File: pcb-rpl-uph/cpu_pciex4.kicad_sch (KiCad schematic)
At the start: 3 parts, among them U5 RPL_UPH_FCBGA1744

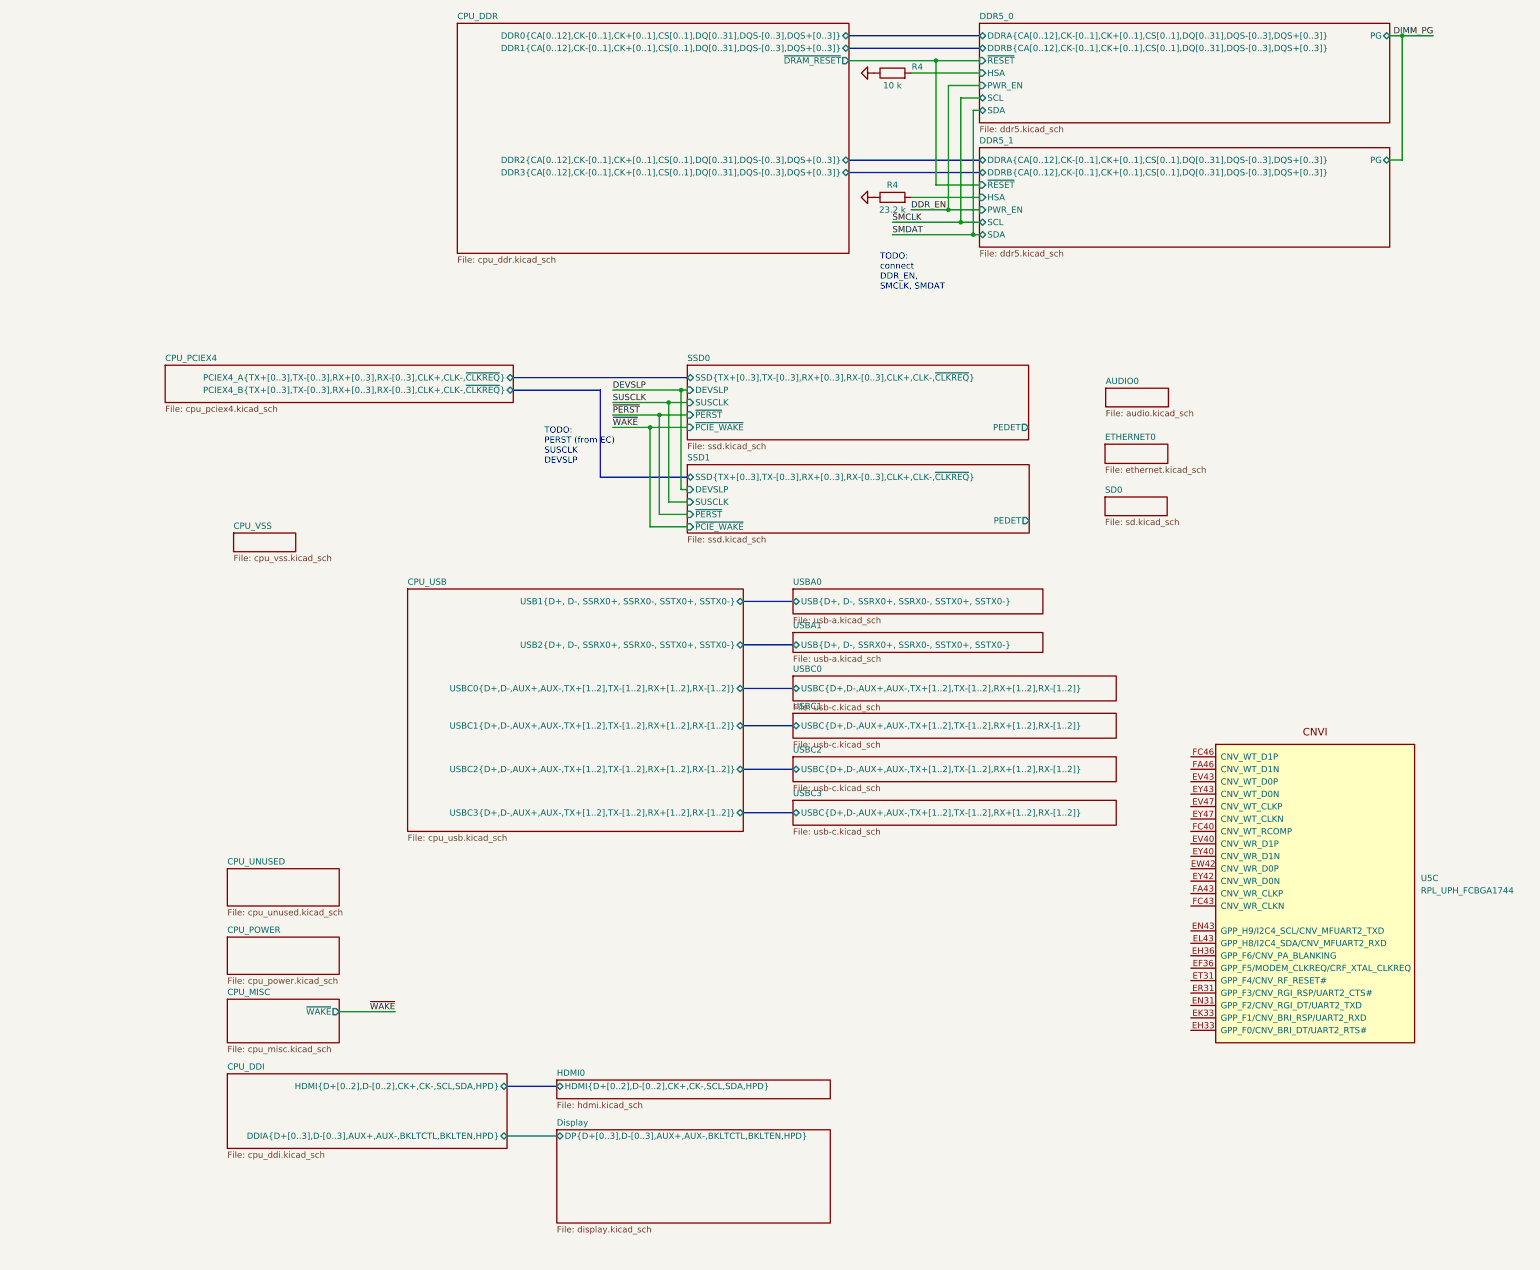
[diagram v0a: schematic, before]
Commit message: refactor much of CPU schematic symbol
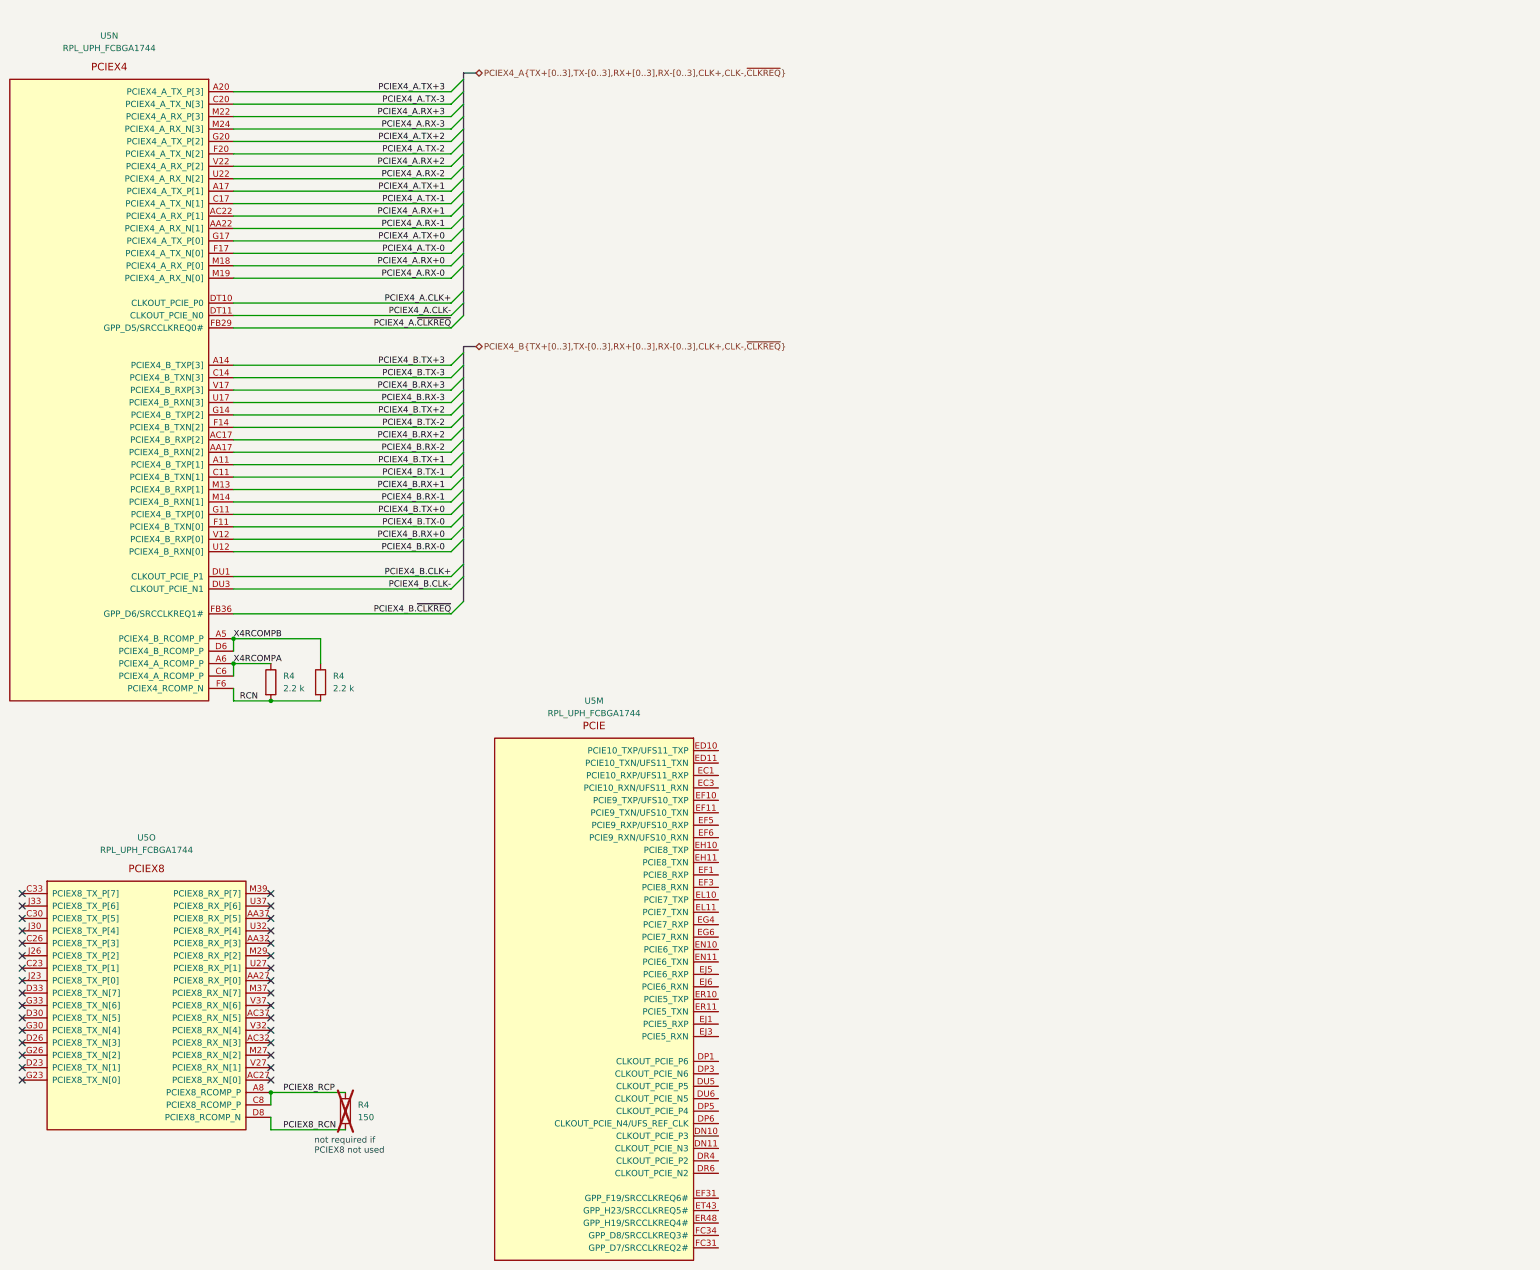
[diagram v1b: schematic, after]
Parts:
- removed R4: 23.2 k, local:R_0201_0603Metric, symbol Device:R
- removed R4: 10 k, local:R_0201_0603Metric, symbol Device:R
- removed U5: RPL_UPH_FCBGA1744, local:RPL_UPH_FCBGA1744, symbol local:RPL_UPH_FCBGA1744
- added R4 (x2): 2.2 k, local:R_0201_0603Metric, symbol Device:R
- added R4: 150, local:R_0201_0603Metric, symbol Device:R
- added U5: RPL_UPH_FCBGA1744, local:RPL_UPH_FCBGA1744, symbol local:RPL_UPH_FCBGA1744
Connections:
- new net PCIEX4_A.CLK+: U5.DT10 (CLKOUT_PCIE_P0)
- new net PCIEX4_A.CLK-: U5.DT11 (CLKOUT_PCIE_N0)
- new net PCIEX4_A.RX+0: U5.M18 (PCIEX4_A_RX_P[0])
- new net PCIEX4_A.RX+1: U5.AC22 (PCIEX4_A_RX_P[1])
- new net PCIEX4_A.RX+2: U5.V22 (PCIEX4_A_RX_P[2])
- new net PCIEX4_A.RX+3: U5.M22 (PCIEX4_A_RX_P[3])
- new net PCIEX4_A.RX-0: U5.M19 (PCIEX4_A_RX_N[0])
- new net PCIEX4_A.RX-1: U5.AA22 (PCIEX4_A_RX_N[1])
- new net PCIEX4_A.RX-2: U5.U22 (PCIEX4_A_RX_N[2])
- new net PCIEX4_A.RX-3: U5.M24 (PCIEX4_A_RX_N[3])
- new net PCIEX4_A.TX+0: U5.G17 (PCIEX4_A_TX_P[0])
- new net PCIEX4_A.TX+1: U5.A17 (PCIEX4_A_TX_P[1])
- new net PCIEX4_A.TX+2: U5.G20 (PCIEX4_A_TX_P[2])
- new net PCIEX4_A.TX+3: U5.A20 (PCIEX4_A_TX_P[3])
- new net PCIEX4_A.TX-0: U5.F17 (PCIEX4_A_TX_N[0])
- new net PCIEX4_A.TX-1: U5.C17 (PCIEX4_A_TX_N[1])
- new net PCIEX4_A.TX-2: U5.F20 (PCIEX4_A_TX_N[2])
- new net PCIEX4_A.TX-3: U5.C20 (PCIEX4_A_TX_N[3])
- new net PCIEX4_A.~{CLKREQ}: U5.FB29 (GPP_D5/SRCCLKREQ0#)
- new net PCIEX4_B.CLK+: U5.DU1 (CLKOUT_PCIE_P1)
- new net PCIEX4_B.CLK-: U5.DU3 (CLKOUT_PCIE_N1)
- new net PCIEX4_B.RX+0: U5.V12 (PCIEX4_B_RXP[0])
- new net PCIEX4_B.RX+1: U5.M13 (PCIEX4_B_RXP[1])
- new net PCIEX4_B.RX+2: U5.AC17 (PCIEX4_B_RXP[2])
- new net PCIEX4_B.RX+3: U5.V17 (PCIEX4_B_RXP[3])
- new net PCIEX4_B.RX-0: U5.U12 (PCIEX4_B_RXN[0])
- new net PCIEX4_B.RX-1: U5.M14 (PCIEX4_B_RXN[1])
- new net PCIEX4_B.RX-2: U5.AA17 (PCIEX4_B_RXN[2])
- new net PCIEX4_B.RX-3: U5.U17 (PCIEX4_B_RXN[3])
- new net PCIEX4_B.TX+0: U5.G11 (PCIEX4_B_TXP[0])
- new net PCIEX4_B.TX+1: U5.A11 (PCIEX4_B_TXP[1])
- new net PCIEX4_B.TX+2: U5.G14 (PCIEX4_B_TXP[2])
- new net PCIEX4_B.TX+3: U5.A14 (PCIEX4_B_TXP[3])
- new net PCIEX4_B.TX-0: U5.F11 (PCIEX4_B_TXN[0])
- new net PCIEX4_B.TX-1: U5.C11 (PCIEX4_B_TXN[1])
- new net PCIEX4_B.TX-2: U5.F14 (PCIEX4_B_TXN[2])
- new net PCIEX4_B.TX-3: U5.C14 (PCIEX4_B_TXN[3])
- new net PCIEX4_B.~{CLKREQ}: U5.FB36 (GPP_D6/SRCCLKREQ1#)
- new net PCIEX8_RCN: R4.2, U5.D8 (PCIEX8_RCOMP_N)
- new net PCIEX8_RCP: R4.1, U5.A8 (PCIEX8_RCOMP_P), U5.C8 (PCIEX8_RCOMP_P)
- new net RCN: R4.2, R4.2, U5.F6 (PCIEX4_RCOMP_N)
- new net X4RCOMPA: R4.1, U5.A6 (PCIEX4_A_RCOMP_P), U5.C6 (PCIEX4_A_RCOMP_P)
- new net X4RCOMPB: R4.1, U5.A5 (PCIEX4_B_RCOMP_P), U5.D6 (PCIEX4_B_RCOMP_P)
- no-connect marks 0 -> 32
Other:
- removed sheet AUDIO0
- removed sheet CPU_DDI
- removed sheet CPU_DDR
- removed sheet CPU_MISC
- removed sheet CPU_PCIEX4
- removed sheet CPU_POWER
- removed sheet CPU_UNUSED
- removed sheet CPU_USB
- removed sheet CPU_VSS
- removed sheet DDR5_0
- removed sheet DDR5_1
- removed sheet Display
- removed sheet ETHERNET0
- removed sheet HDMI0
- removed sheet SD0
- removed sheet SSD0
- removed sheet SSD1
- removed sheet USBA0
- removed sheet USBA1
- removed sheet USBC0
- removed sheet USBC1
- removed sheet USBC2
- removed sheet USBC3
- note added: "not required if PCIEX8 not used"
- note removed: "TODO: PERST (from EC) SUSCLK DEVSLP"
- note removed: "TODO: connect DDR_EN, SMCLK, SMDAT"

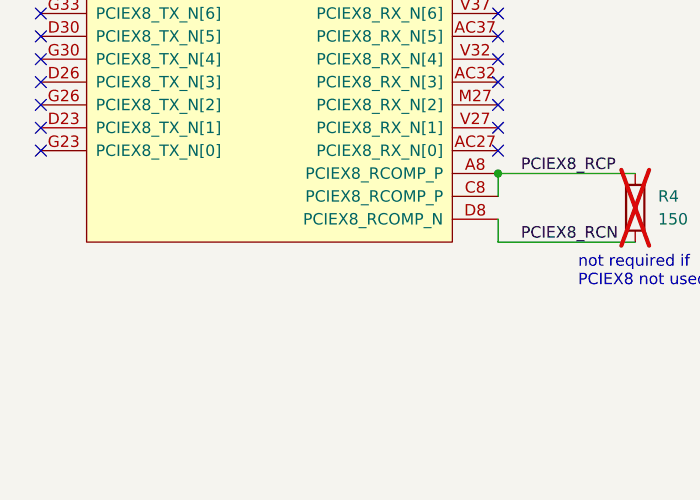
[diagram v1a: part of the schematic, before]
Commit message: charger work in progress also adds 1.1, 1.8 V supplies
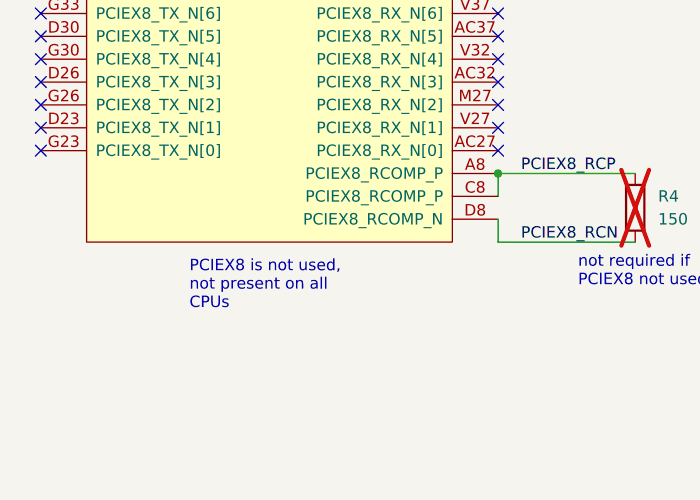
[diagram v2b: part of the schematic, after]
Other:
- note added: "PCIEX8 is not used, not present on all CPUs"
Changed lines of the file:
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@@
+    (effects (font (size 1.27 1.27)) (justify left bottom))
+  )
+  (text "PCIEX8 is not used,\nnot present on all\nCPUs" (at 38.1 248.92 0)
     (effects (font (size 1.27 1.27)) (justify left bottom))
   )
